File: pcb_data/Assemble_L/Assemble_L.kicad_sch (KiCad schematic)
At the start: 75 parts, among them U1 XIAO-nRF52840

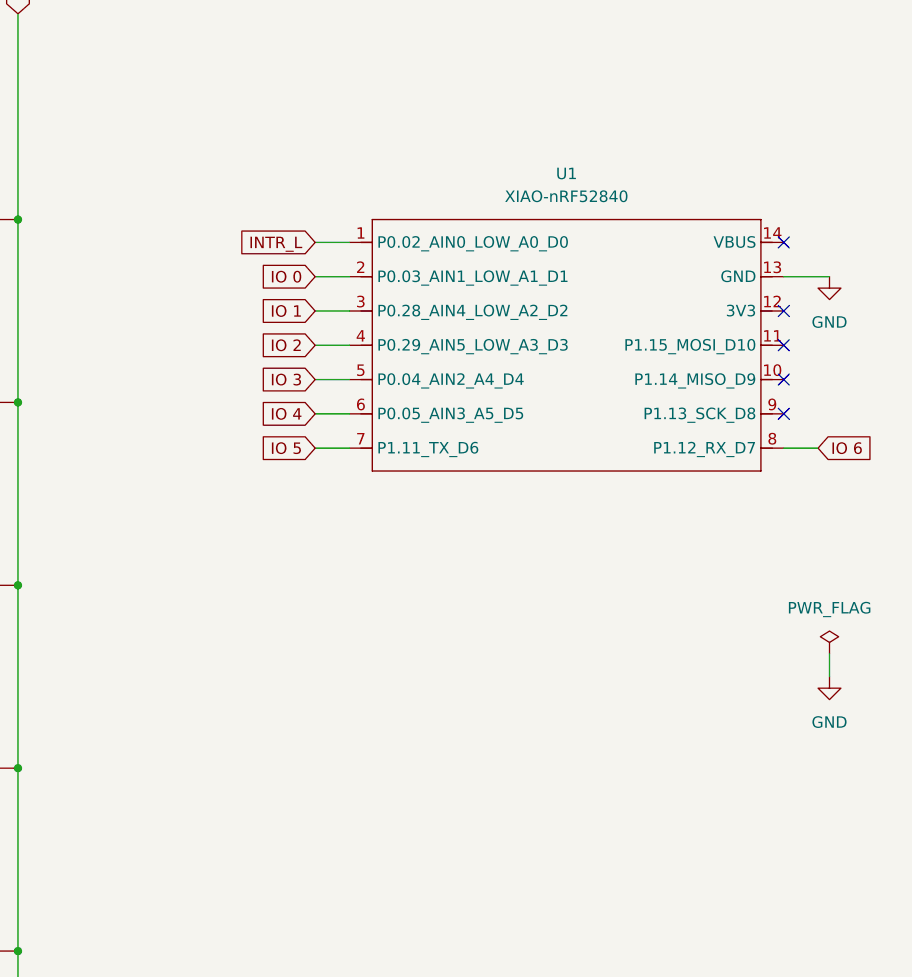
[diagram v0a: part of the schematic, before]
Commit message: replace symbol of xiao-ble
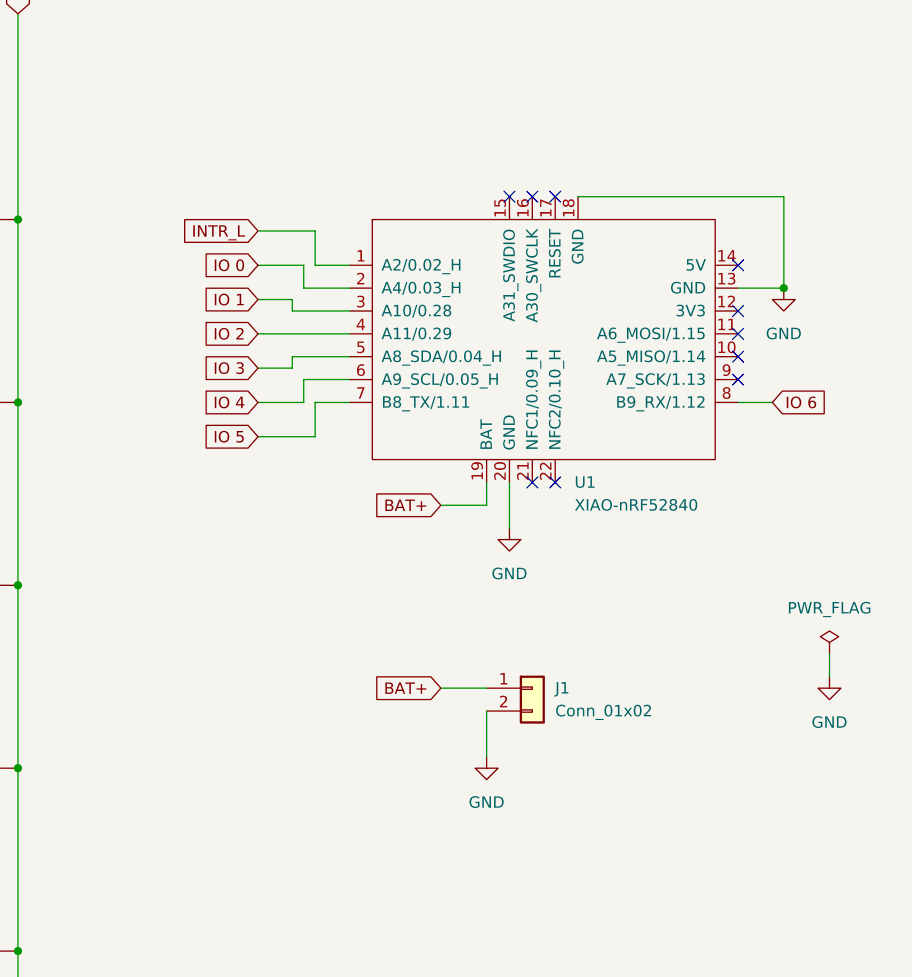
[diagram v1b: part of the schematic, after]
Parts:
- added J1: Conn_01x02, Connector_JST:JST_PH_B2B-PH-K_1x02_P2.00mm_Vertical, symbol Connector_Generic:Conn_01x02
- U1: footprint Seeed Studio XIAO Series Library:XIAO-nRF52840-DIP -> mcu:xiao-ble-smd-cutout; symbol Seeed_Studio_XIAO_Series:XIAO-nRF52840-DIP -> mcu:xiao-ble
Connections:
- net GND: now also U1.18 (GND), U1.20 (GND), J1.2 (Pin_2)
- new net BAT+: J1.1 (Pin_1), U1.19 (BAT)
- no-connect marks 5 -> 10
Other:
- moved on the sheet: U1

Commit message: add component-class field
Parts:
- U1: Component Class (none) -> CastellatedModule
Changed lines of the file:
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@@
+			)
+		)
+		(property "Component Class" "CastellatedModule"
+			(at 234.95 63.5 0)
+			(effects
+				(font
+					(size 1.27 1.27)
+				)
+				(hide yes)
 			)
 		)

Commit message: Issue/14 change hole position (#22)
* add kbd_hole lib

* add mount hole component

* add mount hole, and fix patterns

* project file updated

* add mounting holes schematics

* step files updates

* Issue/21 add capacitor bat gnd (#23)

* add Capacitor symbol

* add Capacitor foot print

* project file updated

* add model number of capacitor

* tune hole positions

* step files updates

* add model number of capacitor

* Feat/fix power line width (#24)

* fix power line pattern width

* project file updated

* tune hole position near by xiao

* step files updated
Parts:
- added C1: GRM32EC81C476KE15L, Capacitor_SMD:C_1210_3225Metric_Pad1.33x2.70mm_HandSolder, symbol Device:C
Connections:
- net BAT+: now also C1.1
- net GND: now also C1.2
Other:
- added sheet MountingHoles (MountingHoles.kicad_sch)
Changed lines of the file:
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@@
 	)
 	(junction
+		(at 226.06 82.55)
+		(diameter 0)
+		(color 0 0 0 0)
+	)
+	(junction
 		(at 95.25 83.82)
 		(diameter 0)
@@
 	)
 	(junction
+		(at 231.14 90.17)
+		(diameter 0)
+		(color 0 0 0 0)
+	)
+	(junction
 		(at 34.29 83.82)
 		(diameter 0)
@@
 	(wire
 		(pts
+			(xy 226.06 90.17) (xy 231.14 90.17)
+		)
+		(stroke
+			(width 0)
+			(type default)
+		)
+	)
+	(wire
+		(pts
 			(xy 223.52 102.87) (xy 228.6 102.87)
 		)
@@
 	(wire
 		(pts
-			(xy 223.52 82.55) (xy 228.6 82.55)
+			(xy 223.52 82.55) (xy 226.06 82.55)
 		)
 		(stroke
@@
 	(wire
 		(pts
+			(xy 231.14 80.01) (xy 231.14 90.17)
+		)
+		(stroke
+			(width 0)
+			(type default)
+		)
+	)
+	(wire
+		(pts
 			(xy 54.61 104.14) (xy 54.61 124.46)
 		)
@@
 	(wire
 		(pts
-			(xy 44.45 50.8) (xy 64.77 50.8)
+			(xy 231.14 90.17) (xy 231.14 92.71)
 		)
 		(stroke
@@
 	(wire
 		(pts
-			(xy 74.93 83.82) (xy 74.93 104.14)
+			(xy 44.45 50.8) (xy 64.77 50.8)
 		)
 		(stroke
@@
 	(wire
 		(pts
-			(xy 231.14 80.01) (xy 231.14 85.09)
+			(xy 74.93 83.82) (xy 74.93 104.14)
 		)
 		(stroke
@@
 	(wire
 		(pts
+			(xy 226.06 82.55) (xy 228.6 82.55)
+		)
+		(stroke
+			(width 0)
+			(type default)
+		)
+	)
+	(wire
+		(pts
 			(xy 74.93 43.18) (xy 74.93 63.5)
 		)
@@
 	(symbol
 		(lib_id "power:GND")
-		(at 231.14 85.09 0)
+		(at 231.14 92.71 0)
 		(unit 1)
 		(exclude_from_sim no)
@@
 		(fields_autoplaced yes)
 		(property "Reference" "#PWR02"
-			(at 231.14 91.44 0)
+			(at 231.14 99.06 0)
 			(effects
 				(font
@@
 		)
 		(property "Value" "GND"
-			(at 231.14 90.17 0)
+			(at 231.14 97.79 0)
 			(effects
 				(font
@@
 		)
 		(property "Footprint" ""
-			(at 231.14 85.09 0)
+			(at 231.14 92.71 0)
 			(effects
 				(font
@@
 		)
 		(property "Datasheet" ""
-			(at 231.14 85.09 0)
+			(at 231.14 92.71 0)
 			(effects
 				(font
@@
 		)
 		(property "Description" "Power symbol creates a global label with name \"GND\" , ground"
-			(at 231.14 85.09 0)
+			(at 231.14 92.71 0)
 			(effects
 				(font
@@
 	)
 	(symbol
+		(lib_id "Device:C")
+		(at 226.06 86.36 0)
+		(unit 1)
+		(exclude_from_sim no)
+		(in_bom yes)
+		(on_board yes)
+		(dnp no)
+		(property "Reference" "C1"
+			(at 220.98 86.106 0)
+			(effects
+				(font
+					(size 1.27 1.27)
+				)
+				(justify left)
+			)
+		)
+		(property "Value" "GRM32EC81C476KE15L"
+			(at 221.488 88.9 0)
+			(effects
+				(font
+					(size 1.27 1.27)
+				)
+				(justify left)
+				(hide yes)
+			)
+		)
+		(property "Footprint" "Capacitor_SMD:C_1210_3225Metric_Pad1.33x2.70mm_HandSolder"
+			(at 227.0252 90.17 0)
+			(effects
+				(font
+					(size 1.27 1.27)
+				)
+				(hide yes)
+			)
+		)
+		(property "Datasheet" "~"
+			(at 226.06 86.36 0)
+			(effects
+				(font
+					(size 1.27 1.27)
+				)
+				(hide yes)
+			)
+		)
+		(property "Description" "Unpolarized capacitor"
+			(at 226.06 86.36 0)
+			(effects
+				(font
+					(size 1.27 1.27)
+				)
+				(hide yes)
+			)
+		)
+		(pin "1"
+		)
+		(pin "2"
+		)
+		(instances
+			(project ""
+				(path "/e3283b87-c43c-4022-8f4a-8d39acdeb3e4"
+					(reference "C1")
+					(unit 1)
+				)
+			)
+		)
+	)
+	(symbol
 		(lib_id "power:GND")
 		(at 228.6 110.49 0)
@@
 				)
 			)
+		)
+	)
+	(sheet
+		(at 190.5 120.65)
+		(size 88.9 6.35)
+		(exclude_from_sim no)
+		(in_bom yes)
+		(on_board yes)
+		(dnp no)
+		(fields_autoplaced yes)
+		(stroke
+			(width 0.1524)
+			(type solid)
+		)
+		(fill
+			(color 0 0 0 0.0000)
+		)
+		(property "Sheetname" "MountingHoles"
+			(at 190.5 119.9384 0)
+			(effects
+				(font
+					(size 1.27 1.27)
+				)
+				(justify left bottom)
+			)
+		)
+		(property "Sheetfile" "MountingHoles.kicad_sch"
+			(at 190.5 127.5846 0)
+			(effects
+				(font
+					(size 1.27 1.27)
+				)
+				(justify left top)
+			)
+		)
+		(instances
+			(project "Assemble_L"
+				(path "/e3283b87-c43c-4022-8f4a-8d39acdeb3e4"
+					(page "2")
+				)
+			)
